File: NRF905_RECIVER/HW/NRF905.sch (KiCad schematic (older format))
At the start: 19 parts

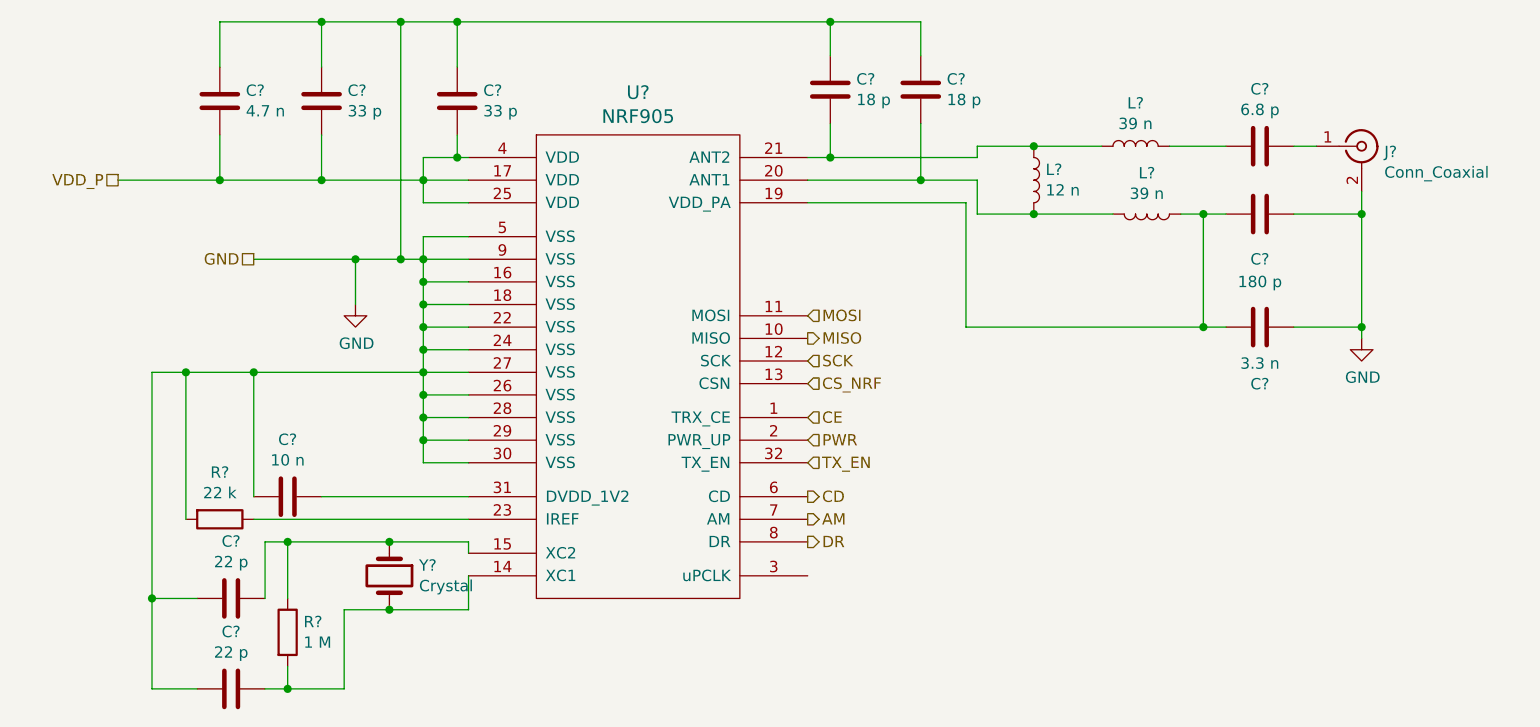
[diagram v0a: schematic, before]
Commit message: Изменение в схемотехнике приемника. Добавлен TFT модуль, WIFI модуль.
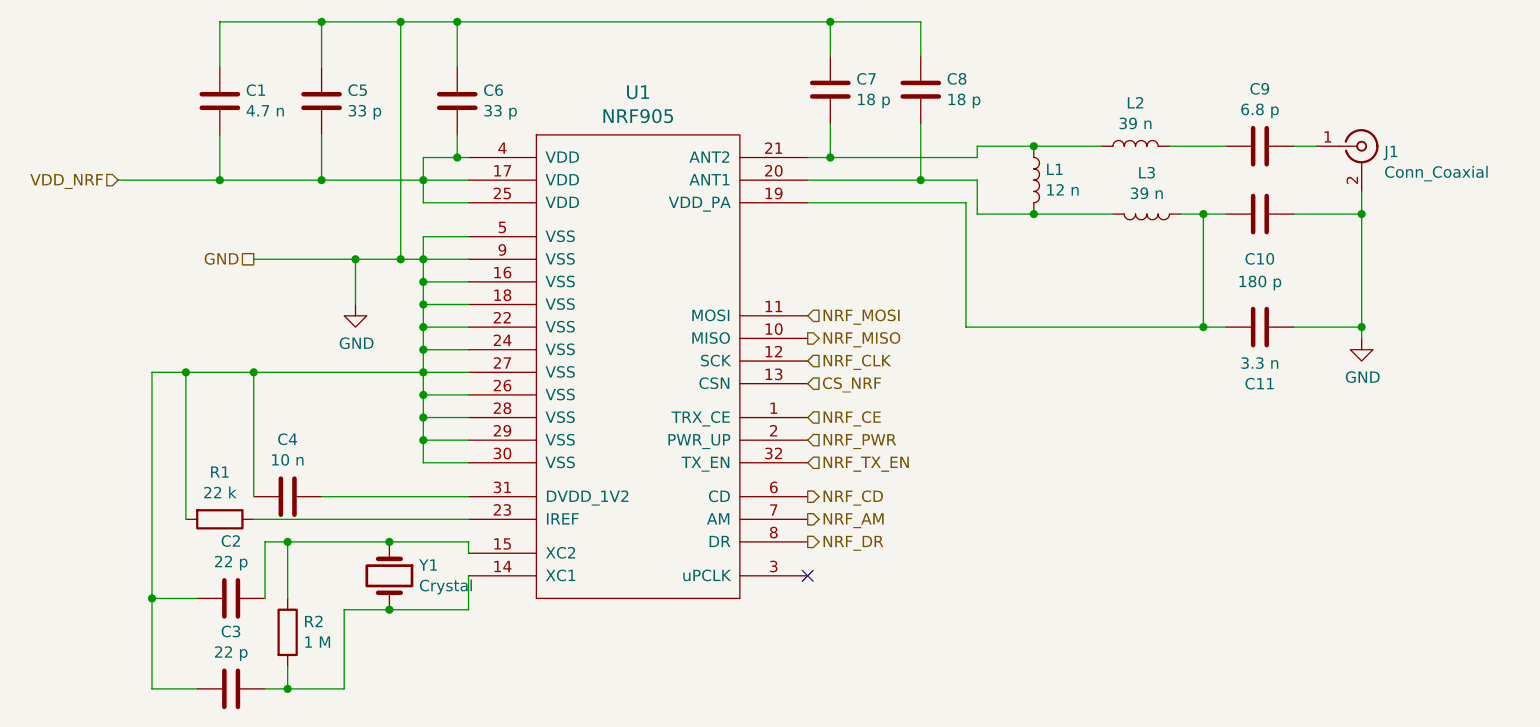
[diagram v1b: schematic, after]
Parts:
- C1, C10, C11, C2, C3, C4, C5, C6, C7, C8, C9: renamed from C?; footprint Capacitor_SMD:C_0402_1005Metric -> Capacitor_SMD:C_0603_1608Metric_Pad1.05x0.95mm_HandSolder
- L1, L2, L3: renamed from L?; footprint Inductor_SMD:L_0402_1005Metric -> Inductor_SMD:L_0603_1608Metric_Pad1.05x0.95mm_HandSolder
- R1, R2: renamed from R?; footprint Resistor_SMD:R_0402_1005Metric -> Resistor_SMD:R_0603_1608Metric_Pad1.05x0.95mm_HandSolder
- gave numbers to parts that had none: 3
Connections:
- net AM renamed NRF_AM
- net CD renamed NRF_CD
- net CE renamed NRF_CE
- net DR renamed NRF_DR
- net MISO renamed NRF_MISO
- net MOSI renamed NRF_MOSI
- net PWR renamed NRF_PWR
- net SCK renamed NRF_CLK
- net TX_EN renamed NRF_TX_EN
- net VDD_P renamed VDD_NRF
- no-connect marks 0 -> 1
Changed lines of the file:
@@
 $Descr A4 11693 8268
 encoding utf-8
-Sheet 3 3
+Sheet 3 5
 Title ""
 Date ""
@@
 	3250 2700 3250 1650
 $Comp
-L Device:C C?
+L Device:C C4
 U 1 1 5EBD35B2
 P 2750 3750
-F 0 "C?" V 2498 3750 50  0000 C CNN
+F 0 "C4" V 2498 3750 50  0000 C CNN
 F 1 "10 n" V 2589 3750 50  0000 C CNN
-F 2 "Capacitor_SMD:C_0402_1005Metric" H 2788 3600 50  0001 C CNN
+F 2 "Capacitor_SMD:C_0603_1608Metric_Pad1.05x0.95mm_HandSolder" H 2788 3600 50  0001 C CNN
 F 3 "~" H 2750 3750 50  0001 C CNN
 	1    2750 3750
@@
 	2900 3750 3550 3750
 $Comp
-L Device:R R?
+L Device:R R1
 U 1 1 5EBD35BB
 P 2450 3850
-F 0 "R?" V 2243 3850 50  0000 C CNN
+F 0 "R1" V 2243 3850 50  0000 C CNN
 F 1 "22 k" V 2334 3850 50  0000 C CNN
-F 2 "Resistor_SMD:R_0402_1005Metric" V 2380 3850 50  0001 C CNN
+F 2 "Resistor_SMD:R_0603_1608Metric_Pad1.05x0.95mm_HandSolder" V 2380 3850 50  0001 C CNN
 F 3 "~" H 2450 3850 50  0001 C CNN
 	1    2450 3850
@@
 	3550 3850 2600 3850
 $Comp
-L Device:C C?
+L Device:C C5
 U 1 1 5EBD35D0
 P 2900 2000
-F 0 "C?" H 3015 2046 50  0000 L CNN
+F 0 "C5" H 3015 2046 50  0000 L CNN
 F 1 "33 p" H 3015 1955 50  0000 L CNN
-F 2 "Capacitor_SMD:C_0402_1005Metric" H 2938 1850 50  0001 C CNN
+F 2 "Capacitor_SMD:C_0603_1608Metric_Pad1.05x0.95mm_HandSolder" H 2938 1850 50  0001 C CNN
 F 3 "~" H 2900 2000 50  0001 C CNN
 	1    2900 2000
@@
 $EndComp
 $Comp
-L Device:C C?
+L Device:C C1
 U 1 1 5EBD35D6
 P 2450 2000
-F 0 "C?" H 2565 2046 50  0000 L CNN
+F 0 "C1" H 2565 2046 50  0000 L CNN
 F 1 "4.7 n" H 2565 1955 50  0000 L CNN
-F 2 "Capacitor_SMD:C_0402_1005Metric" H 2488 1850 50  0001 C CNN
+F 2 "Capacitor_SMD:C_0603_1608Metric_Pad1.05x0.95mm_HandSolder" H 2488 1850 50  0001 C CNN
 F 3 "~" H 2450 2000 50  0001 C CNN
 	1    2450 2000
@@
 Connection ~ 3250 1650
 $Comp
-L Device:L L?
+L Device:L L2
 U 1 1 5EBD35F3
 P 6500 2200
-F 0 "L?" V 6690 2200 50  0000 C CNN
+F 0 "L2" V 6690 2200 50  0000 C CNN
 F 1 "39 n" V 6599 2200 50  0000 C CNN
-F 2 "Inductor_SMD:L_0402_1005Metric" H 6500 2200 50  0001 C CNN
+F 2 "Inductor_SMD:L_0603_1608Metric_Pad1.05x0.95mm_HandSolder" H 6500 2200 50  0001 C CNN
 F 3 "~" H 6500 2200 50  0001 C CNN
 	1    6500 2200
@@
 $EndComp
 $Comp
-L Device:L L?
+L Device:L L3
 U 1 1 5EBD35F9
 P 6550 2500
-F 0 "L?" V 6369 2500 50  0000 C CNN
+F 0 "L3" V 6369 2500 50  0000 C CNN
 F 1 "39 n" V 6460 2500 50  0000 C CNN
-F 2 "Inductor_SMD:L_0402_1005Metric" H 6550 2500 50  0001 C CNN
+F 2 "Inductor_SMD:L_0603_1608Metric_Pad1.05x0.95mm_HandSolder" H 6550 2500 50  0001 C CNN
 F 3 "~" H 6550 2500 50  0001 C CNN
 	1    6550 2500
@@
 $EndComp
 $Comp
-L Device:L L?
+L Device:L L1
 U 1 1 5EBD35FF
 P 6050 2350
-F 0 "L?" H 6102 2396 50  0000 L CNN
+F 0 "L1" H 6102 2396 50  0000 L CNN
 F 1 "12 n" H 6102 2305 50  0000 L CNN
-F 2 "Inductor_SMD:L_0402_1005Metric" H 6050 2350 50  0001 C CNN
+F 2 "Inductor_SMD:L_0603_1608Metric_Pad1.05x0.95mm_HandSolder" H 6050 2350 50  0001 C CNN
 F 3 "~" H 6050 2350 50  0001 C CNN
 	1    6050 2350
@@
 	5800 2350 5800 2500
 $Comp
-L Device:C C?
+L Device:C C11
 U 1 1 5EBD3611
 P 7050 3000
-F 0 "C?" V 6798 3000 50  0000 C CNN
+F 0 "C11" V 6798 3000 50  0000 C CNN
 F 1 "3.3 n" V 6889 3000 50  0000 C CNN
-F 2 "Capacitor_SMD:C_0402_1005Metric" H 7088 2850 50  0001 C CNN
+F 2 "Capacitor_SMD:C_0603_1608Metric_Pad1.05x0.95mm_HandSolder" H 7088 2850 50  0001 C CNN
 F 3 "~" H 7050 3000 50  0001 C CNN
 	1    7050 3000
@@
 	5050 2450 5750 2450
 $Comp
-L Device:C C?
+L Device:C C10
 U 1 1 5EBD3622
 P 7050 2500
-F 0 "C?" V 7250 2500 50  0000 C CNN
+F 0 "C10" V 7250 2500 50  0000 C CNN
 F 1 "180 p" V 7350 2500 50  0000 C CNN
-F 2 "Capacitor_SMD:C_0402_1005Metric" H 7088 2350 50  0001 C CNN
+F 2 "Capacitor_SMD:C_0603_1608Metric_Pad1.05x0.95mm_HandSolder" H 7088 2350 50  0001 C CNN
 F 3 "~" H 7050 2500 50  0001 C CNN
 	1    7050 2500
@@
 $EndComp
 $Comp
-L Device:C C?
+L Device:C C8
 U 1 1 5EBD362D
 P 5550 1950
-F 0 "C?" H 5665 1996 50  0000 L CNN
+F 0 "C8" H 5665 1996 50  0000 L CNN
 F 1 "18 p" H 5665 1905 50  0000 L CNN
-F 2 "Capacitor_SMD:C_0402_1005Metric" H 5588 1800 50  0001 C CNN
+F 2 "Capacitor_SMD:C_0603_1608Metric_Pad1.05x0.95mm_HandSolder" H 5588 1800 50  0001 C CNN
 F 3 "~" H 5550 1950 50  0001 C CNN
 	1    5550 1950
@@
 $EndComp
 $Comp
-L Device:C C?
+L Device:C C7
 U 1 1 5EBD3633
 P 5150 1950
-F 0 "C?" H 5265 1996 50  0000 L CNN
+F 0 "C7" H 5265 1996 50  0000 L CNN
 F 1 "18 p" H 5265 1905 50  0000 L CNN
-F 2 "Capacitor_SMD:C_0402_1005Metric" H 5188 1800 50  0001 C CNN
+F 2 "Capacitor_SMD:C_0603_1608Metric_Pad1.05x0.95mm_HandSolder" H 5188 1800 50  0001 C CNN
 F 3 "~" H 5150 1950 50  0001 C CNN
 	1    5150 1950
@@
 $EndComp
 $Comp
-L Connector:Conn_Coaxial J?
+L Connector:Conn_Coaxial J1
 U 1 1 5EBD363F
 P 7500 2200
-F 0 "J?" H 7600 2175 50  0000 L CNN
+F 0 "J1" H 7600 2175 50  0000 L CNN
 F 1 "Conn_Coaxial" H 7600 2084 50  0000 L CNN
 F 2 "Connector_Coaxial:U.FL_Molex_MCRF_73412-0110_Vertical" H 7500 2200 50  0001 C CNN
@@
 	2450 2150 2450 2350
 $Comp
-L power:GND #PWR?
+L power:GND #PWR0101
 U 1 1 5EBED4BE
 P 7500 3050
-F 0 "#PWR?" H 7500 2800 50  0001 C CNN
+F 0 "#PWR0101" H 7500 2800 50  0001 C CNN
 F 1 "GND" H 7505 2877 50  0000 C CNN
 F 2 "" H 7500 3050 50  0001 C CNN
@@
 Connection ~ 2450 2350
 Text HLabel 5050 3050 2    50   Output ~ 0
-MISO
+NRF_MISO
 Text HLabel 5050 2950 2    50   Input ~ 0
-MOSI
+NRF_MOSI
 Text HLabel 5050 3150 2    50   Input ~ 0
-SCK
+NRF_CLK
 Text HLabel 5050 3250 2    50   Input ~ 0
 CS_NRF
 Text HLabel 5050 3400 2    50   Input ~ 0
-CE
+NRF_CE
 Text HLabel 5050 3500 2    50   Input ~ 0
-PWR
+NRF_PWR
 Text HLabel 5050 3600 2    50   Input ~ 0
-TX_EN
+NRF_TX_EN
 Text HLabel 5050 3750 2    50   Output ~ 0
-CD
+NRF_CD
 Text HLabel 5050 3850 2    50   Output ~ 0
-AM
+NRF_AM
 Text HLabel 5050 3950 2    50   Output ~ 0
-DR
+NRF_DR
 Text HLabel 2600 2700 0    50   UnSpc ~ 0
 GND
-Text HLabel 2000 2350 0    50   UnSpc ~ 0
-VDD_P
 Wire Wire Line
 	2000 2350 2450 2350
@@
 	2600 2700 3050 2700
 $Comp
-L _wireless:NRF905 U?
+L _wireless:NRF905 U1
 U 1 1 5EBD3534
 P 4300 3200
-F 0 "U?" H 4300 4437 60  0000 C CNN
+F 0 "U1" H 4300 4437 60  0000 C CNN
 F 1 "NRF905" H 4300 4331 60  0000 C CNN
 F 2 "Package_DFN_QFN:QFN-32-1EP_5x5mm_P0.5mm_EP3.6x3.6mm" H 4300 3150 60  0001 C CNN
@@
 $EndComp
 $Comp
-L Device:C C?
+L Device:C C6
 U 1 1 5EBD35C5
 P 3500 2000
-F 0 "C?" H 3615 2046 50  0000 L CNN
+F 0 "C6" H 3615 2046 50  0000 L CNN
 F 1 "33 p" H 3615 1955 50  0000 L CNN
-F 2 "Capacitor_SMD:C_0402_1005Metric" H 3538 1850 50  0001 C CNN
+F 2 "Capacitor_SMD:C_0603_1608Metric_Pad1.05x0.95mm_HandSolder" H 3538 1850 50  0001 C CNN
 F 3 "~" H 3500 2000 50  0001 C CNN
 	1    3500 2000
@@
 	3550 4250 3550 4100
 $Comp
-L Device:C C?
+L Device:C C2
 U 1 1 5EB90A98
 P 2500 4200
-F 0 "C?" V 2248 4200 50  0000 C CNN
+F 0 "C2" V 2248 4200 50  0000 C CNN
 F 1 "22 p" V 2339 4200 50  0000 C CNN
-F 2 "Capacitor_SMD:C_0402_1005Metric" H 2538 4050 50  0001 C CNN
+F 2 "Capacitor_SMD:C_0603_1608Metric_Pad1.05x0.95mm_HandSolder" H 2538 4050 50  0001 C CNN
 F 3 "~" H 2500 4200 50  0001 C CNN
 	1    2500 4200
@@
 $EndComp
 $Comp
-L Device:C C?
+L Device:C C3
 U 1 1 5EB917BB
 P 2500 4600
-F 0 "C?" V 2248 4600 50  0000 C CNN
+F 0 "C3" V 2248 4600 50  0000 C CNN
 F 1 "22 p" V 2339 4600 50  0000 C CNN
-F 2 "Capacitor_SMD:C_0402_1005Metric" H 2538 4450 50  0001 C CNN
+F 2 "Capacitor_SMD:C_0603_1608Metric_Pad1.05x0.95mm_HandSolder" H 2538 4450 50  0001 C CNN
 F 3 "~" H 2500 4600 50  0001 C CNN
 	1    2500 4600
@@
 Connection ~ 2150 4200
 $Comp
-L Device:R R?
+L Device:R R2
 U 1 1 5EB9E4FF
 P 2750 4350
-F 0 "R?" H 2820 4396 50  0000 L CNN
+F 0 "R2" H 2820 4396 50  0000 L CNN
 F 1 "1 M" H 2820 4305 50  0000 L CNN
-F 2 "Resistor_SMD:R_0402_1005Metric" V 2680 4350 50  0001 C CNN
+F 2 "Resistor_SMD:R_0603_1608Metric_Pad1.05x0.95mm_HandSolder" V 2680 4350 50  0001 C CNN
 F 3 "~" H 2750 4350 50  0001 C CNN
 	1    2750 4350
@@
 	2750 4600 3000 4600
 $Comp
-L power:GND #PWR?
+L power:GND #PWR0102
 U 1 1 5EBEDA90
 P 3050 2900
-F 0 "#PWR?" H 3050 2650 50  0001 C CNN
+F 0 "#PWR0102" H 3050 2650 50  0001 C CNN
 F 1 "GND" H 3055 2727 50  0000 C CNN
 F 2 "" H 3050 2900 50  0001 C CNN
@@
 	3000 4250 3200 4250
 $Comp
-L Device:Crystal Y?
+L Device:Crystal Y1
 U 1 1 5EB6F079
 P 3200 4100
-F 0 "Y?" V 3154 4231 50  0000 L CNN
+F 0 "Y1" V 3154 4231 50  0000 L CNN
 F 1 "Crystal" V 3245 4231 50  0000 L CNN
 F 2 "Crystal:Crystal_SMD_TXC_7A-2Pin_5x3.2mm" H 3200 4100 50  0001 C CNN
@@
 	6800 3000 6900 3000
 $Comp
-L Device:C C?
+L Device:C C9
 U 1 1 5EBD361C
 P 7050 2200
-F 0 "C?" V 6798 2200 50  0000 C CNN
+F 0 "C9" V 6798 2200 50  0000 C CNN
 F 1 "6.8 p" V 6889 2200 50  0000 C CNN
-F 2 "Capacitor_SMD:C_0402_1005Metric" H 7088 2050 50  0001 C CNN
+F 2 "Capacitor_SMD:C_0603_1608Metric_Pad1.05x0.95mm_HandSolder" H 7088 2050 50  0001 C CNN
 F 3 "~" H 7050 2200 50  0001 C CNN
 	1    7050 2200
@@
 Wire Wire Line
 	5800 2200 6050 2200
+NoConn ~ 5050 4100
+Text HLabel 2000 2350 0    50   Input ~ 0
+VDD_NRF
 $EndSCHEMATC

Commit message: new scematics. New PCB.
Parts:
- U1: symbol _wireless:NRF905 -> RECIVER_NRF-rescue:NRF905-_wireless
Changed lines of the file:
@@
 	2600 2700 3050 2700
 $Comp
-L _wireless:NRF905 U1
+L RECIVER_NRF-rescue:NRF905-_wireless U1
 U 1 1 5EBD3534
 P 4300 3200
